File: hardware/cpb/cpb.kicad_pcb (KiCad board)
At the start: 6 copper layers, 95.9 x 90.2 mm, 237 parts, among them J1 Conn_02x20_Odd_Even, J10 SW1, J11 SW2, J12 SW3, J13 PISW1, J14 μSW1, J15 μSW2, J16 μSW3, J17 μSW4, J2 I2CExt, J3 DAC1BUF, J4 DAC2BUF, J6 Conn_02x20_Odd_Even, J7 ADC6/7, J8 ADC2/3, J9 4FBRG, J99 RBFJUMP, Q1 PMBT2222A, Q10 BSS138PS,115, Q11 BSS138PS,115, Q12 MBT2222ADW1T1, Q13 MBT2222ADW1T1, Q14 BSS138PS,115, Q15 BSS138PS,115, Q16 MBT2222ADW1T1, Q17 MBT2222ADW1T1, Q18 BSS138PS,115, Q19 BSS138PS,115, Q2 IRF9393, Q20 MBT2222ADW1T1, Q21 MBT2222ADW1T1, Q22 BSS138PS,115, Q23 BSS138PS,115, Q24 MBT2222ADW1T1, Q25 IRF7306, Q26 MBT2222ADW1T1, Q27 IRF7306, Q28 MBT2222ADW1T1, Q29 IRF7306, Q3 MBT2222ADW1T1, Q30 MBT2222ADW1T1, Q31 IRF7306, Q4 PMBT2222A, Q5 PMBT2222A, Q6 IRF9393, Q7 PMBT2222A, Q8 MBT2222ADW1T1, Q9 MBT2222ADW1T1, U1 TS912, U2 ADR420ARMZ, U3 KF33BDT, U4 STM32L072R_B-Z_Tx, U5 AP62301WU, U6 SC16IS750xBS, U7 SC18IS606, U8 KF33BDT, U9 MAX22200, Y1 14.7456MHz

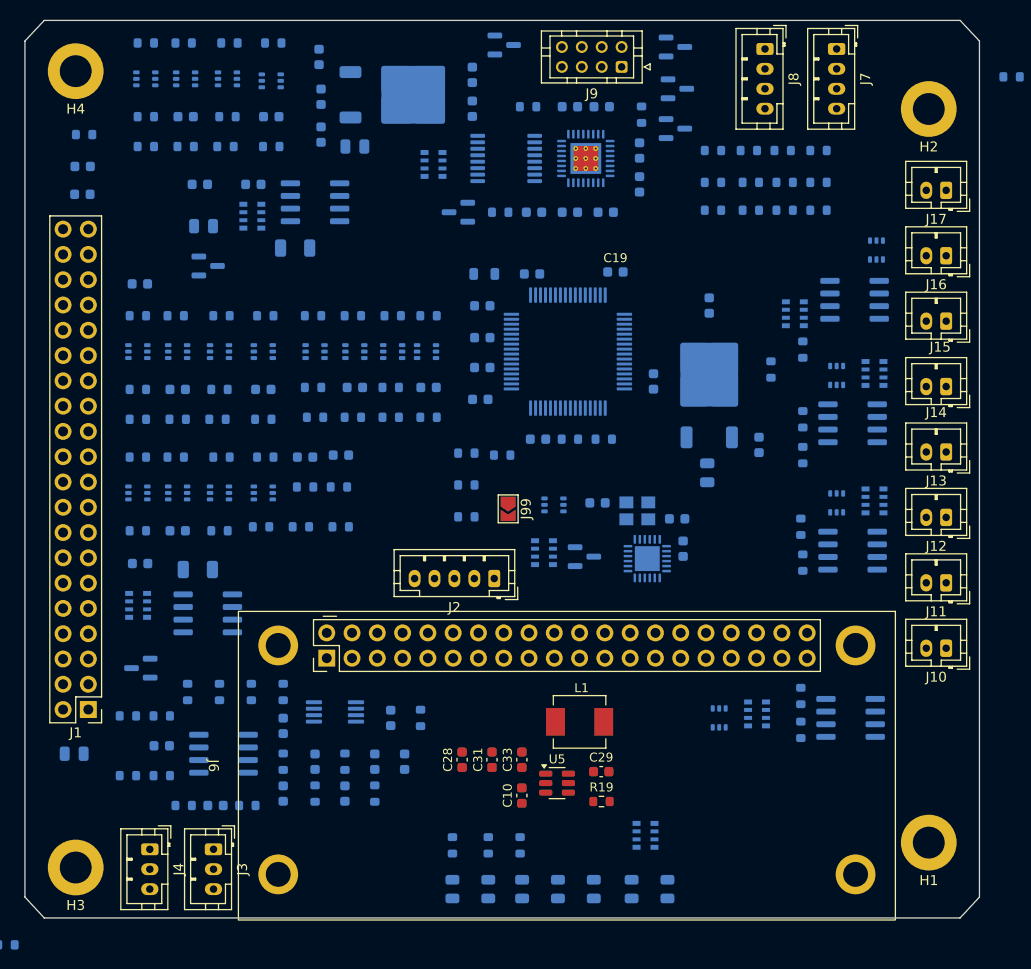
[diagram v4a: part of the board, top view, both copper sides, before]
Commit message: hardware/cpb: slight moves to text and grid alignment
Adjusted text locations as well as began aligning grid.
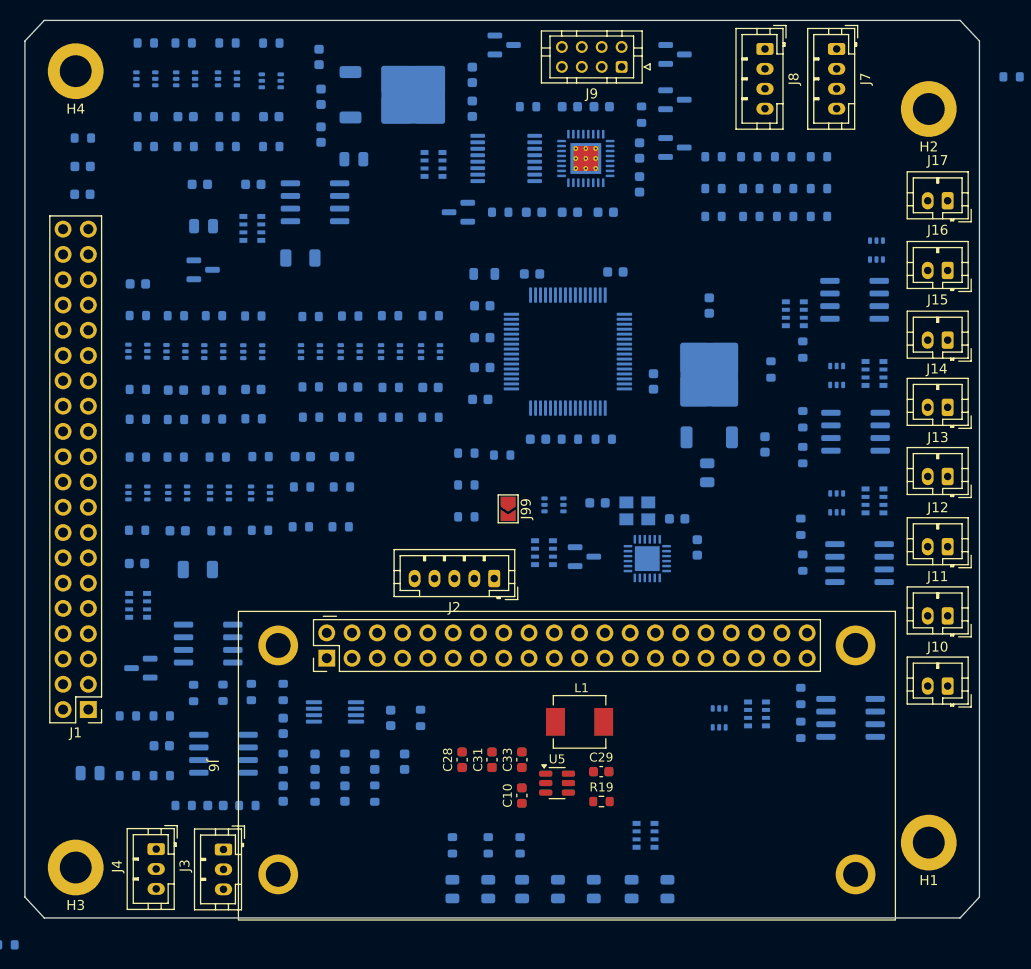
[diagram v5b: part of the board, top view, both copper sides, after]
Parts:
- moved J10 3.80 mm to (193.6, 125.1)
- moved J11 3.32 mm to (193.6, 118.0)
- moved Q2 3.04 mm to (119.3, 120.8)
- moved J12 2.95 mm to (193.6, 111.1)
- moved C3 2.52 mm to (107.4, 133.8)
- moved J13 2.47 mm to (193.6, 104.0)
- moved J14 2.09 mm to (193.6, 97.1)
- moved J15 1.91 mm to (193.6, 90.3)
- moved D10 1.90 mm to (166.2, 71.0)
- moved J16 1.49 mm to (193.6, 83.3)
- moved Q27 1.43 mm to (184.7, 112.8)
- moved C20 1.43 mm to (168.4, 111.2)
- moved C38 1.28 mm to (133.9, 72.2)
- moved RN9 1.22 mm to (123.7, 79.1)
- moved R73 1.20 mm to (123.8, 87.9)
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
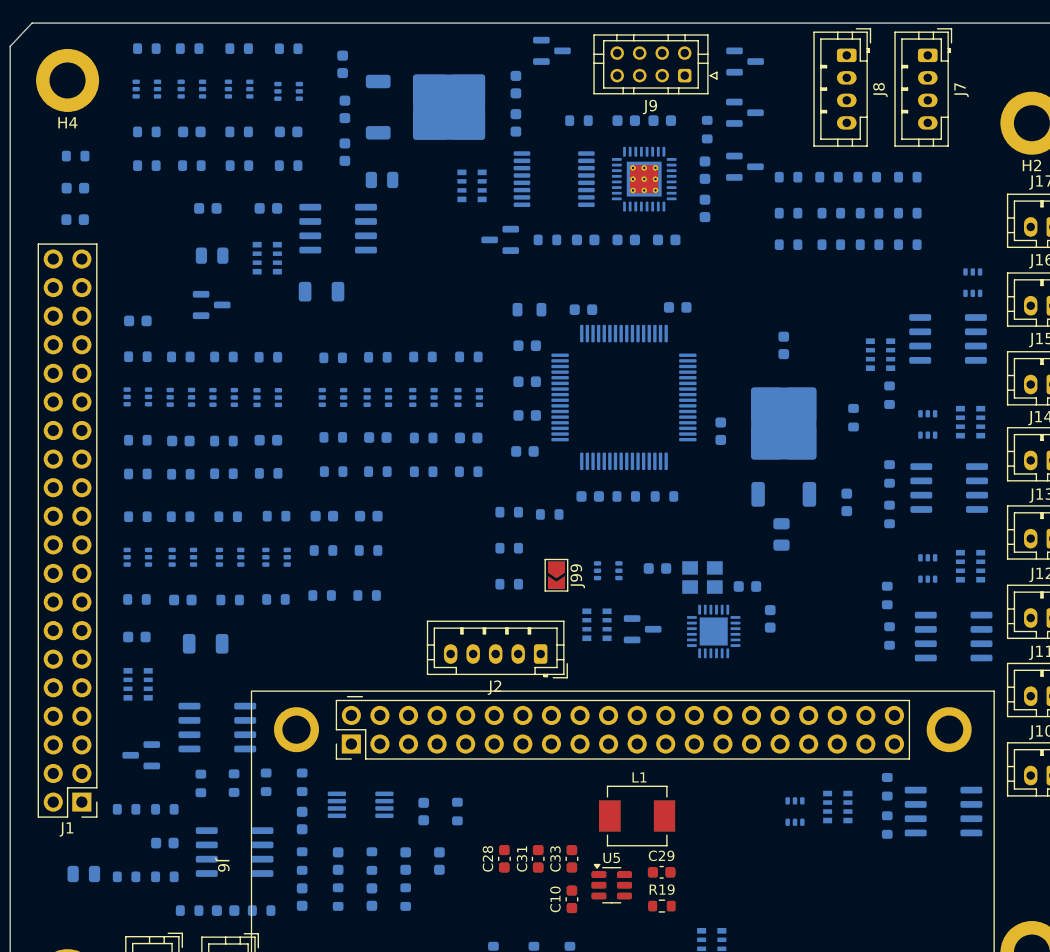
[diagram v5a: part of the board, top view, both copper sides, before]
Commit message: hardware/cpb: more text alignment on cpb and grid work
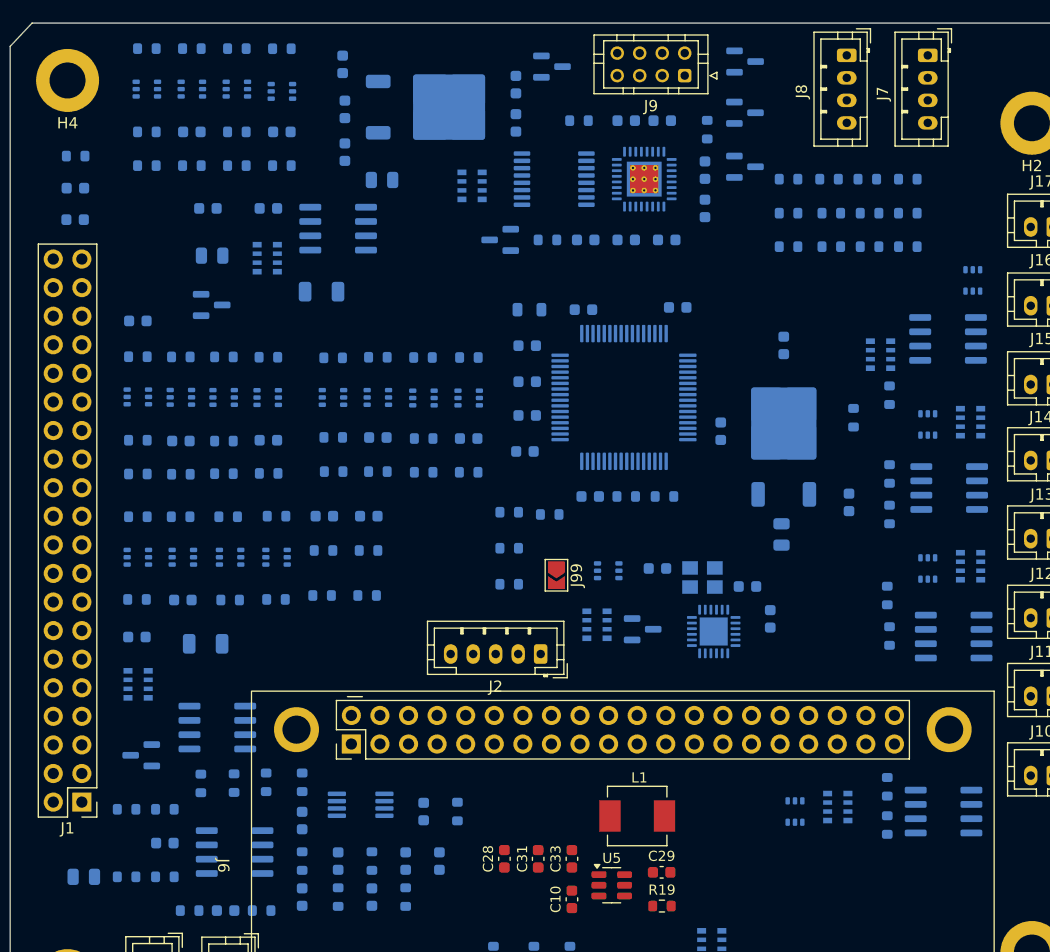
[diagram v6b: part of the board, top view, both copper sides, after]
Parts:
- moved D11 1.40 mm to (149.0, 62.1)
- moved R63 0.61 mm to (125.0, 60.5)
- moved C52 0.60 mm to (125.0, 67.9)
- moved Q11 0.60 mm to (125.0, 64.3)
- moved R61 0.60 mm to (125.0, 70.9)
- moved C3 0.25 mm to (107.4, 134.1)
- moved R59 0.22 mm to (121.0, 70.9)
- moved C14 0.20 mm to (175.4, 100.8)
- moved Q30 0.20 mm to (186.4, 81.1)
- moved Q9 0.20 mm to (121.0, 64.1)
- moved R57 0.20 mm to (121.0, 67.9)
- moved R62 0.20 mm to (117.0, 60.5)
- moved R65 0.20 mm to (121.0, 60.5)
- moved R25 0.17 mm to (177.2, 78.1)
- moved R27 0.17 mm to (180.6, 78.1)
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
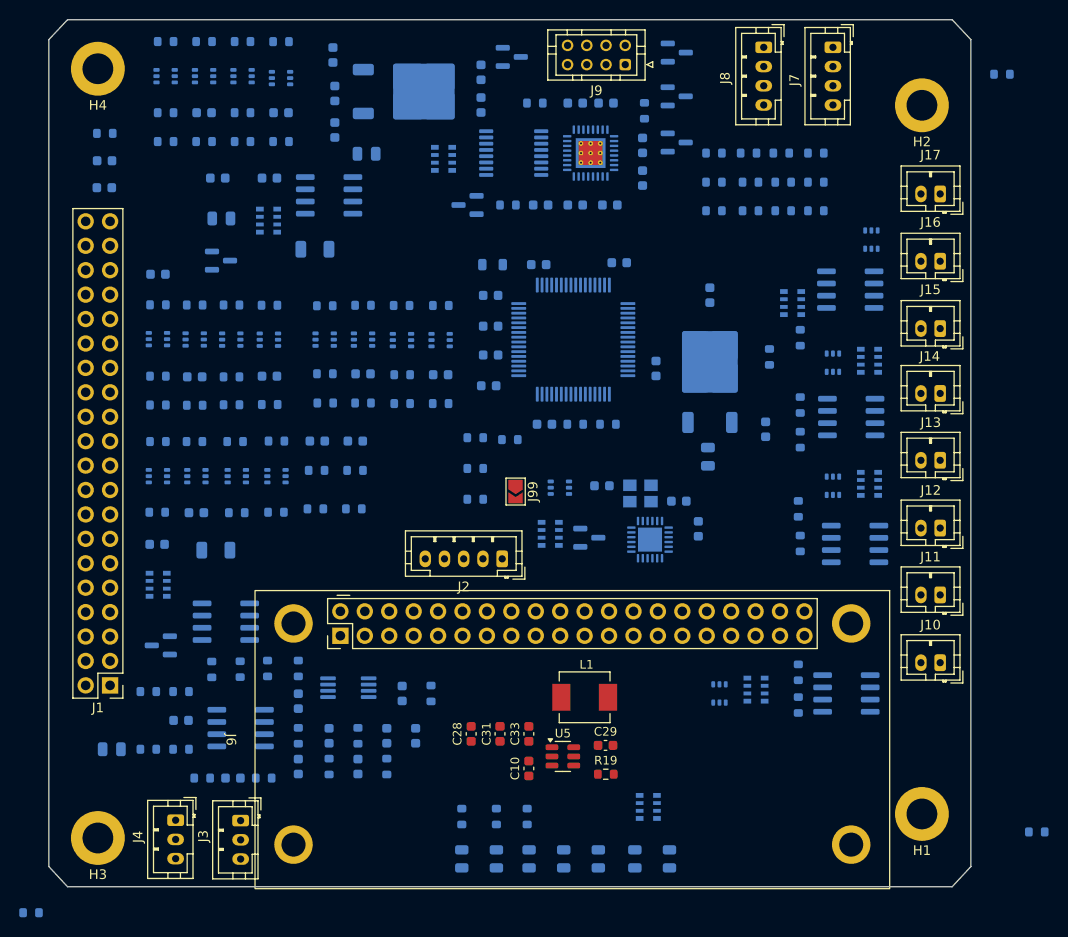
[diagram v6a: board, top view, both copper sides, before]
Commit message: cpb: complete placement
- add a capacitor to ensure we can bypass all 3V3 components well
- align components
- add copper pour regions
- a lot of effort on text, and legends for connectors

Plus probably much more...
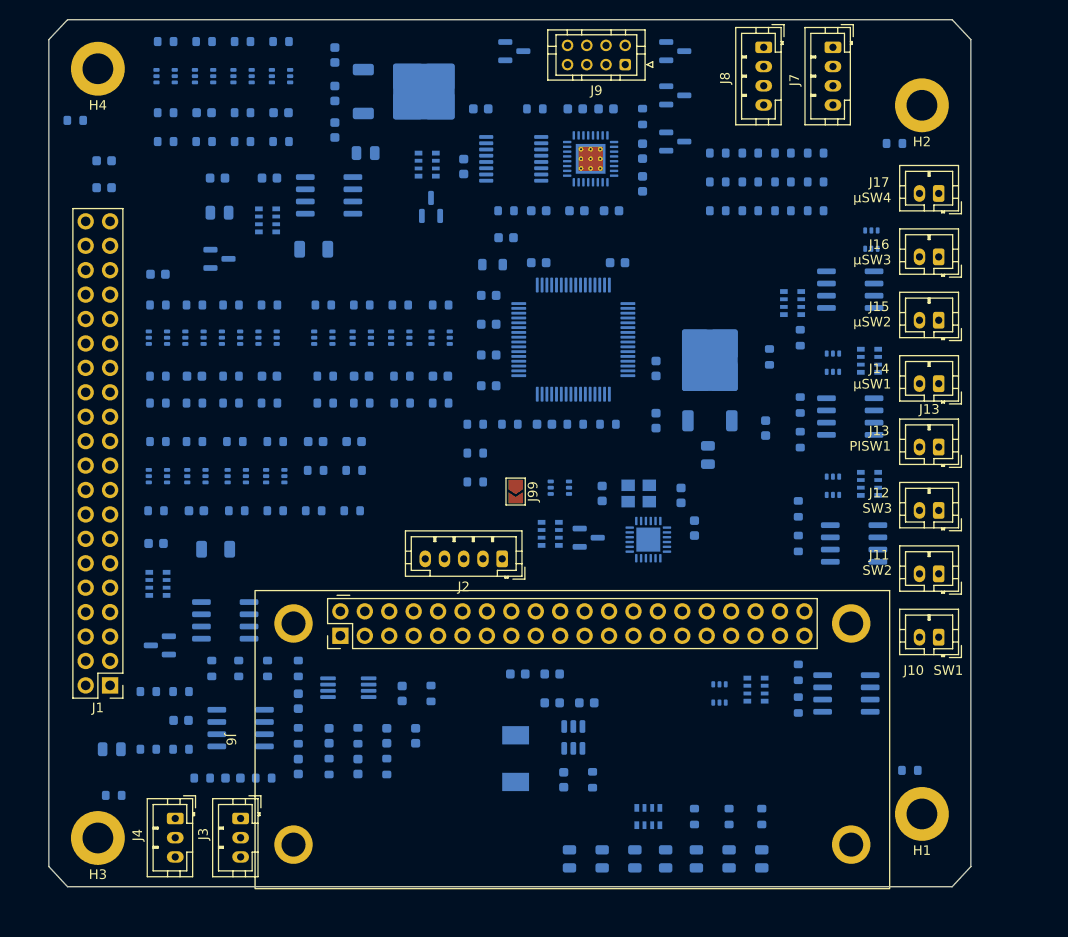
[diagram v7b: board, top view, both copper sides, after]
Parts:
- added C59: 100nF, Capacitor_SMD:C_0603_1608Metric, B.Cu at (164.0, 99.9)
- C10, C28, C29, C31, C33, L1, R19, U5: moved to B.Cu
- moved D1 31.2 mm to (175.0, 145.5)
- moved R22 31.2 mm to (175.0, 141.1)
- moved D2 24.2 mm to (171.6, 145.5)
- moved R23 24.2 mm to (171.6, 141.1)
- moved C32 22.0 mm to (148.4, 80.9), turned to 180 degrees
- moved R28 17.4 mm to (168.0, 141.1)
- moved D3 17.4 mm to (168.2, 145.5)
- moved R42 14.9 mm to (107.6, 138.9)
- moved R40 14.7 mm to (190.4, 136.3)
- moved R41 13.3 mm to (188.8, 71.1)
- moved D4 10.6 mm to (165.0, 145.5)
- moved D7 10.4 mm to (155.0, 145.5)
- moved L1 9.60 mm to (149.4, 135.1), turned to 90 degrees
- moved C10 9.11 mm to (156.8, 129.3), turned to 180 degrees
- moved C31 8.26 mm to (153.2, 126.3), turned to 0 degrees
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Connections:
- J6 pad 2: Net-(J6-Pin_2) -> +5V
- J6 pad 4: Net-(J6-Pin_2) -> +5V
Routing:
- added copper zone on In1.Cu, net +3.3V
- added copper zone on In1.Cu, net +5V
- added copper zone on In1.Cu, net +7.5V
- added copper zone on In1.Cu, net +BATT
- added copper zone on In1.Cu, net /FourFullBridges/FBRDG3V3
- added copper zone on In1.Cu, net /FourFullBridges/VM
- added copper zone on In2.Cu, net GND

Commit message: hardware/cpp: continue layout work
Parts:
- moved J3 1.00 mm to (119.8, 141.3)
- moved C18 0.19 mm to (120.0, 136.9)
- moved R11 0.19 mm to (123.2, 136.9)
- moved R16 0.19 mm to (116.8, 136.9)
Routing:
- net /FourFullBridges/~{CS}: track 0.00 -> 17.4 mm, vias 0 -> 3
- net /FourFullBridges/MISO: track 0.00 -> 12.3 mm, vias 0 -> 2
- net /FourFullBridges/SCK: track 0.00 -> 11.5 mm, vias 0 -> 2
- net /FourFullBridges/MOSI: track 0.00 -> 10.5 mm, vias 0 -> 3
- net GND: track 0.00 -> 10.4 mm, vias 0 -> 34
- net /FourFullBridges/CMD: track 0.00 -> 8.06 mm, vias 0 -> 2
- net /FourFullBridges/FBRDG3V3: track 0.00 -> 2.21 mm, vias 0 -> 16
- net /FourFullBridges/~{REQFBRGEN}: track 0.00 -> 1.82 mm, vias 0 -> 3
- net Net-(U7-~{INT}): track 0.00 -> 1.74 mm, vias 0 -> 2
- net /FourFullBridges/PCVTSDA: track 0.00 -> 1.38 mm, vias 0 -> 3
- net /FourFullBridges/PCVTSCL: track 0.00 -> 1.35 mm, vias 0 -> 3
- net Net-(RN8D-R4.1): track 0.00 -> 1.28 mm, vias 0 -> 2
- net Net-(U9-V_{CP}): vias 0 -> 1
- net Net-(U9-V_{18}): vias 0 -> 1
- net Net-(U9-IREF): vias 0 -> 1
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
